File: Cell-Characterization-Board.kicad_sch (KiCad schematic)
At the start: 5 parts, among them IC2 INA4180A2IPWR, SW1 SW_Push, U1 ESP32-S3-WROOM-1

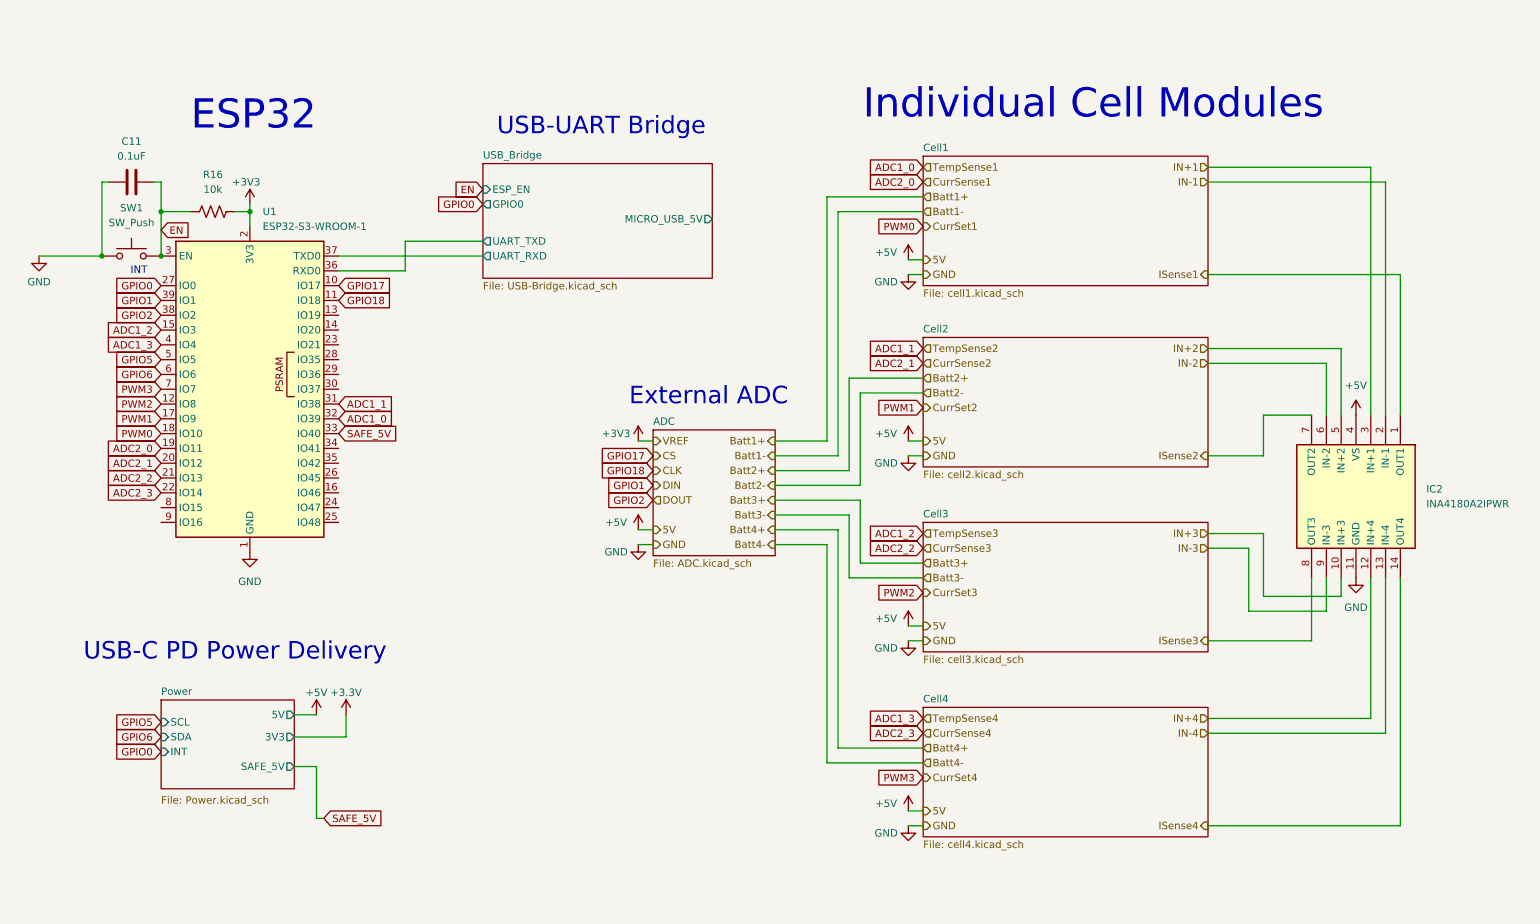
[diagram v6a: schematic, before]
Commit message: me when the power is muxing and pinning esp32
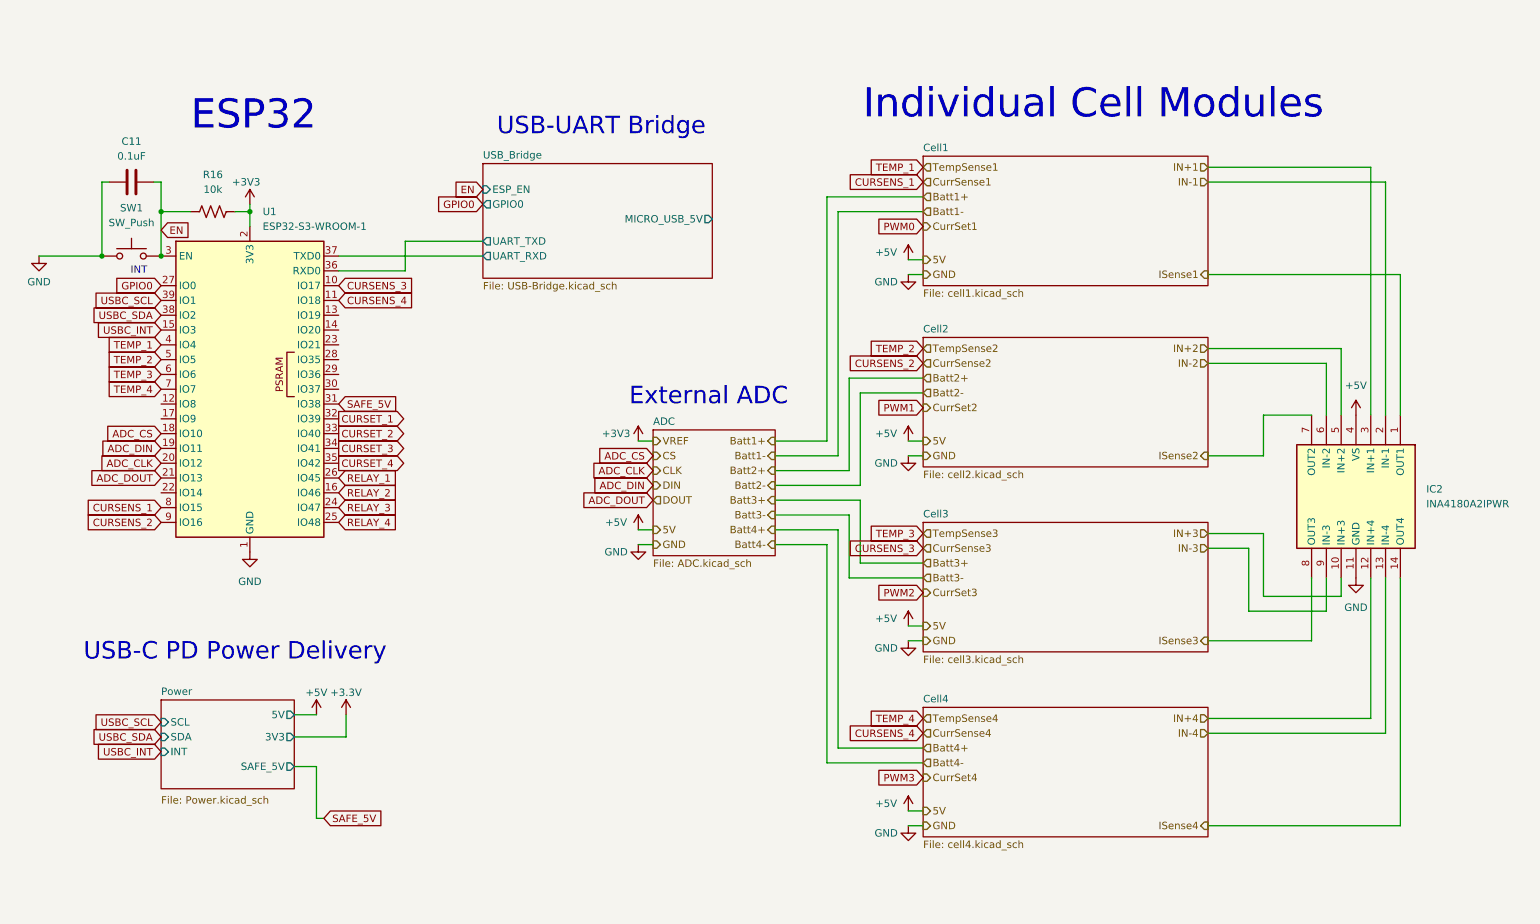
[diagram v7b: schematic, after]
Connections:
- net ADC1_1 is gone; now on net SAFE_5V: U1.31 (IO38)
- net PWM0: no longer U1.18 (IO10)
- net PWM1: no longer U1.17 (IO9)
- net PWM2: no longer U1.12 (IO8)
- net PWM3: no longer U1.7 (IO7)
- net SAFE_5V: no longer U1.33 (IO40)
- net RELAY_2: now reaches U1.16 (IO46)
- net RELAY_3: now reaches U1.24 (IO47)
- net RELAY_4: now reaches U1.25 (IO48)
- net RELAY_1: now reaches U1.26 (IO45)
- net CURSET_3: now reaches U1.34 (IO41)
- net CURSET_4: now reaches U1.35 (IO42)
- net CURSENS_1: now reaches U1.8 (IO15)
- net CURSENS_2: now reaches U1.9 (IO16)
- net ADC1_0 renamed CURSET_1
- net ADC1_2 renamed USBC_INT
- net ADC1_3 renamed TEMP_1
- net ADC2_0 renamed ADC_DIN
- net ADC2_1 renamed ADC_CLK
- net ADC2_2 renamed ADC_DOUT
- net ADC2_3: no longer names the net of U1.22 (IO14)
- net GPIO1 renamed USBC_SCL
- net GPIO17 renamed CURSENS_3
- net GPIO18 renamed CURSENS_4
- net GPIO2 renamed USBC_SDA
- net GPIO5 renamed TEMP_2
- net GPIO6 renamed TEMP_3
- new net ADC_CS: U1.18 (IO10)
- new net CURSET_2: U1.33 (IO40)
- new net TEMP_4: U1.7 (IO7)

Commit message: initial sch completed
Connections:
- net ISense1 is gone; now on net CURSENS_1: IC2.1 (OUT1)
- net ISense2 is gone; now on net CURSENS_2: IC2.7 (OUT2)
- net ISense3 is gone; now on net CURSENS_3: IC2.8 (OUT3)
- net ISense4 is gone; now on net CURSENS_4: IC2.14 (OUT4)
- net IN+1 renamed Cell1/Curr_Sense+
- net IN+2 renamed Cell2/Curr_Sense+
- net IN+3 renamed Cell3/Curr_Sense+
- net IN+4 renamed Cell4/Curr_Sense+
- net IN-1 renamed Cell1/Curr_Sense-
- net IN-2 renamed Cell2/Curr_Sense-
- net IN-3 renamed Cell3/Curr_Sense-
- net IN-4 renamed Cell4/Curr_Sense-
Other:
- sheet Cell1: file cell1.kicad_sch -> cell.kicad_sch
- sheet Cell1 ports: added Batt+, Batt-, CurrSet, Curr_Sense+, Curr_Sense-, I_Sense, Relay, Temp; removed none
- sheet Cell2: file cell2.kicad_sch -> cell.kicad_sch
- sheet Cell2 ports: added Batt+, Batt-, CurrSet, Curr_Sense+, Curr_Sense-, I_Sense, Relay, Temp; removed none
- sheet Cell3: file cell3.kicad_sch -> cell.kicad_sch
- sheet Cell3 ports: added Batt+, Batt-, CurrSet, Curr_Sense+, Curr_Sense-, I_Sense, Relay, Temp; removed none
- sheet Cell4: file cell4.kicad_sch -> cell.kicad_sch
- sheet Cell4 ports: added Batt+, Batt-, CurrSet, Curr_Sense+, Curr_Sense-, I_Sense, Relay, Temp; removed none
